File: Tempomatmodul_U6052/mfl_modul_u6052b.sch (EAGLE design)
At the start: 27 parts, among them IC1 U6052B-A, J1 43045-0800, K1 APF30212C, K2 APF30212C, K3 APF30212C, K4 APF30212C

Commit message: Fixed. Running version!
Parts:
- removed D6: P6KEXXC, diode:P6KEXXC
- removed R11, R12: 665, rcl:R-EU_0207/7
- removed R13: 931, rcl:R-EU_0207/7
- added C3: 100nF, rcl:C-EU025-025X050
- added LED1: led grün 2,2v 20mA, led:LED3MM
- C1: value 100µF -> 1nF
- C2: value 1nF -> 100uF/36V; device rcl:C-EU025-025X050 -> rcl:CPOL-EUE2.5-6
- D1: value BYW52 -> EP20D; device diode:BYW52 -> diode:DIODE-DO15-12
- D2, D3, D4, D5: value CGRM4004-G -> MBSR140; device diode:CGRM4004-G -> Heinrich:SHOTKY-SMDSMB
- J1: value 43045-0800 -> 39-30-1100; device Heinrich:43045-0800 -> Heinrich:39-30-1100
- R1: value 100 -> 560
- R10: value 200 -> 510
- R2: value 510 -> 100
- R3: value 200 -> 200k
- R4: value 270k -> 200
- R5: value 20k -> 931
- R6: value 150k -> 665
- R7: value 39k -> 665
- R8: value 200k -> 200
- R9: value 66.5 -> 66,5
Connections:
- net K1 renamed PLUS
- net K2 renamed ABRUF
- net K3 renamed MINUS
- net K4 renamed I/O
- removed net +12V: D1.C, D2.C, D3.C, D4.C, D5.C, K11.2, K21.2, K31.2, K41.2, R2.1, R3.1, R4.1, R6.1
- removed net LD: IC1.LD, R4.2, R5.2
- removed net MFL_CC: J1.5, R1.1
- removed net N$6: K12.S, K22.S, K32.S, K42.O, R11.1, R13.2
- removed net N$8: K22.P, R10.1
- removed net PO: IC1.PO, R6.2, R7.2
- new net IBUS: J1.3, J1.4
- new net MFL: J1.6, R2.1
- new net N$10: K22.P, R8.1
- new net N$11: K32.P, R7.1
- new net N$12: K12.S, K22.S, K32.S, K42.O, R5.2, R6.1
- new net N$3: LED1.A, R1.1
- new net VCC: D1.C, D2.C, D3.C, D4.C, D5.C, K11.2, K21.2, K31.2, K41.2, R1.2, R10.1, R4.1
- net EML1: now also J1.5, R6.2, R7.2, R8.2; no longer J1.8, R10.2, R11.2, R12.2
- net EML2: now also J1.10, R5.1; no longer J1.4, R13.1
- net GND: now also C2.-, C3.2, IC1.LD, IC1.PO, J1.7, J1.8, J1.9; no longer C2.2, D6.1, J1.2, J1.3, R5.1, R7.1
- net N$1: now also R2.2; no longer R1.2
- net N$2: now also R4.2; no longer R3.2
- net N$4: now also IC1.O8, LED1.C; no longer K32.P, R12.1
- net OSC: now also C1.1, R3.2; no longer C2.1, R8.2
- net VBAT: now also J1.1, J1.2; no longer D6.2, J1.6, J1.7
- net VS: now also C2.+, C3.1, R10.2; no longer C1.1, R2.2
- net VSTAB: now also R3.1; no longer R8.1
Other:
- note added: "logische Ausgänge, 25V und bis 200mA"
- note removed: "Abruf: Bit 1 und 4; 153Ohm Plus: Bit 2 und 5; 66.5Ohm Minus: Bit 7; 332Ohm Aus: 3 und 6; 1590Ohm Leerlauf: NICHTS; 665Ohm"
- note removed: "Anschlüße: 2x EML 2x 12V (rein und raus) 2x GND (rein und raus) 1x Tempomatsignal (rein)"
- note removed: "Wertetabelle: Abruf: K2 auf LOW Plus: K1 auf LOW Minus: K3 auf LOW Aus: K4 auf LOW Leerlauf: alle Relais auf HIGH"

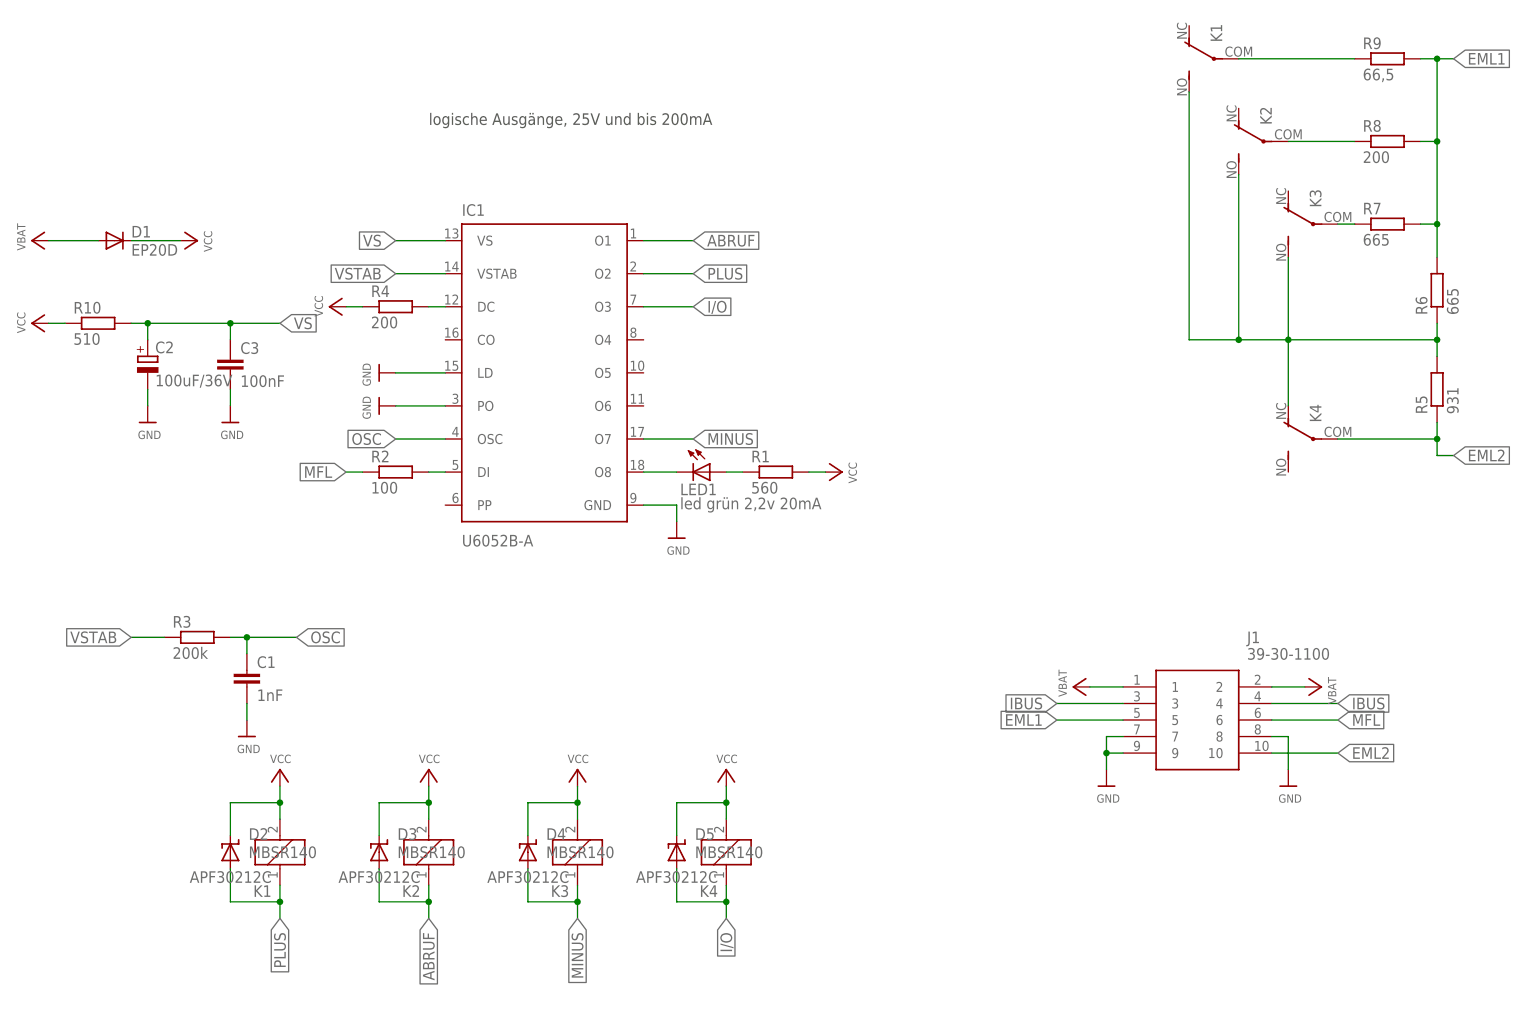
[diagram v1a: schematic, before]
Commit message: Fosc corrected
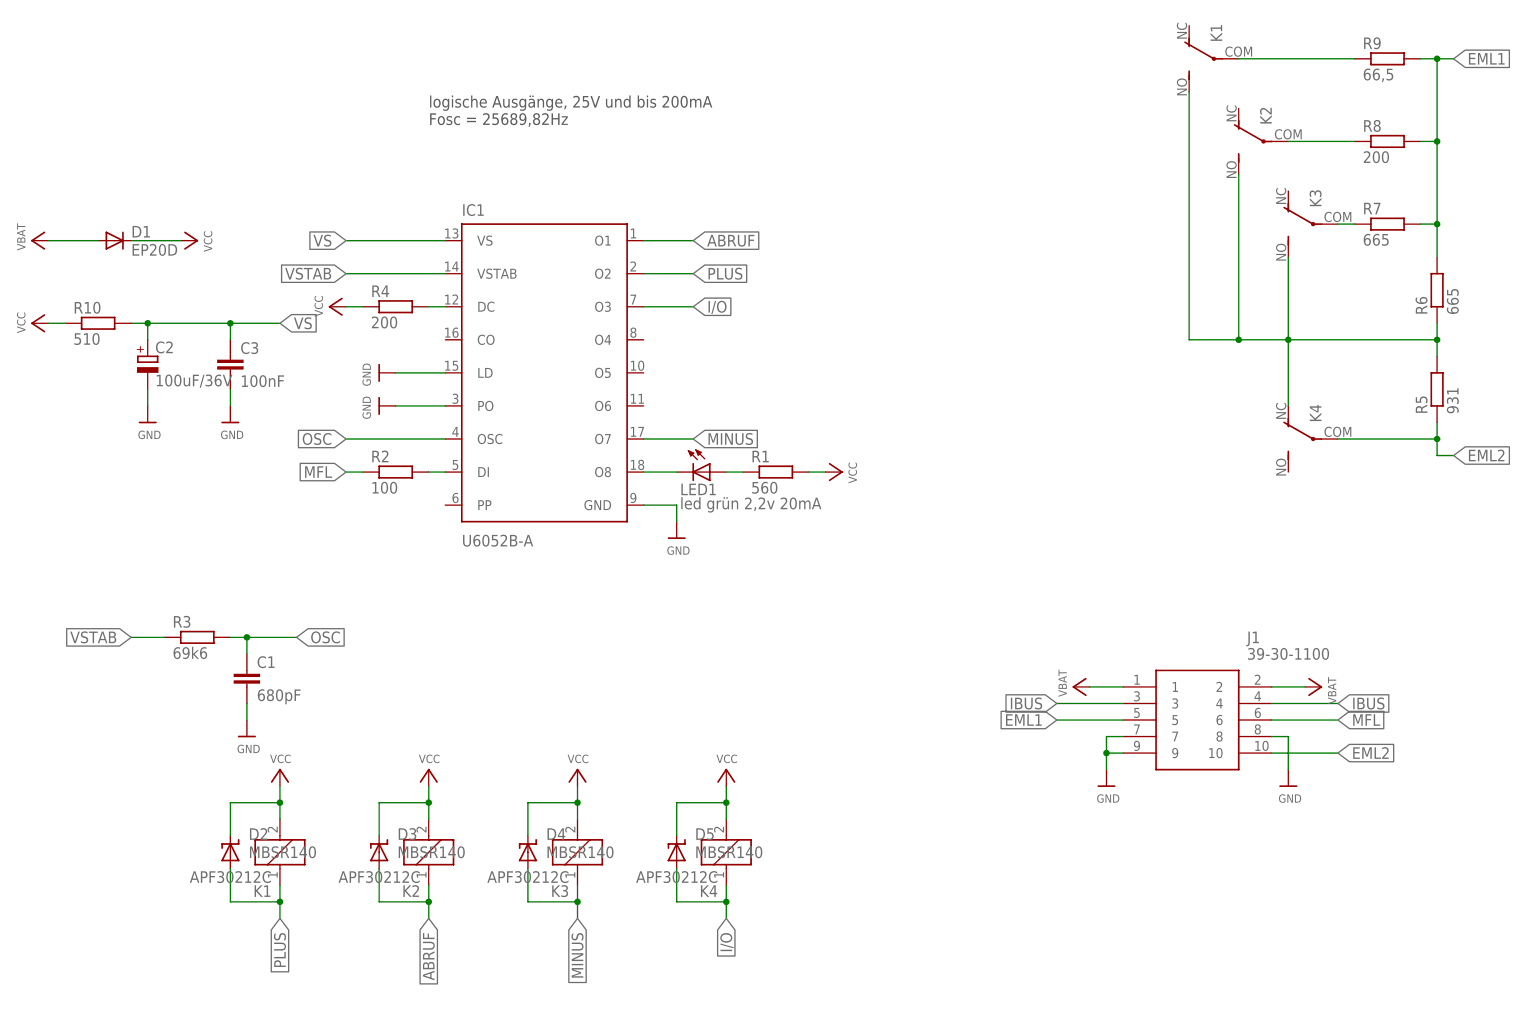
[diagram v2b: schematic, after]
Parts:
- C1: value 1nF -> 680pF
- R3: value 200k -> 69k6
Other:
- note added: "logische Ausgänge, 25V und bis 200mA Fosc = 25689,82Hz"
- note removed: "logische Ausgänge, 25V und bis 200mA"
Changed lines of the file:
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@@
 <setting verticaltext="up"/>
 </settings>
-<grid distance="0.1" unitdist="inch" unit="inch" style="lines" multiple="1" display="no" altdistance="0.01" altunitdist="inch" altunit="inch"/>
+<grid distance="0.1" unitdist="inch" unit="inch" style="lines" multiple="1" display="yes" altdistance="0.01" altunitdist="inch" altunit="inch"/>
 <layers>
 <layer number="1" name="Top" color="4" fill="1" visible="no" active="no"/>
@@
 <part name="R1" library="rcl" library_urn="urn:adsk.eagle:library:334" deviceset="R-EU_" device="0207/7" package3d_urn="urn:adsk.eagle:package:23493/1" value="560"/>
 <part name="P+1" library="microbuilder" deviceset="VCC" device=""/>
-<part name="C1" library="rcl" library_urn="urn:adsk.eagle:library:334" deviceset="C-EU" device="025-025X050" package3d_urn="urn:adsk.eagle:package:23629/2" value="1nF"/>
+<part name="C1" library="rcl" library_urn="urn:adsk.eagle:library:334" deviceset="C-EU" device="025-025X050" package3d_urn="urn:adsk.eagle:package:23629/2" value="680pF"/>
 <part name="R2" library="rcl" library_urn="urn:adsk.eagle:library:334" deviceset="R-EU_" device="0207/7" package3d_urn="urn:adsk.eagle:package:23493/1" value="100"/>
-<part name="R3" library="rcl" library_urn="urn:adsk.eagle:library:334" deviceset="R-EU_" device="0207/7" package3d_urn="urn:adsk.eagle:package:23493/1" value="200k"/>
+<part name="R3" library="rcl" library_urn="urn:adsk.eagle:library:334" deviceset="R-EU_" device="0207/7" package3d_urn="urn:adsk.eagle:package:23493/1" value="69k6"/>
 <part name="R4" library="rcl" library_urn="urn:adsk.eagle:library:334" deviceset="R-EU_" device="0207/7" package3d_urn="urn:adsk.eagle:package:23493/1" value="200"/>
 <part name="R5" library="rcl" library_urn="urn:adsk.eagle:library:334" deviceset="R-EU_" device="0207/7" package3d_urn="urn:adsk.eagle:package:23493/1" value="931"/>
@@
 <sheet>
 <plain>
-<text x="83.82" y="147.32" size="1.778" layer="97">logische Ausgänge, 25V und bis 200mA</text>
+<text x="83.82" y="147.32" size="1.778" layer="97">logische Ausgänge, 25V und bis 200mA
+Fosc = 25689,82Hz</text>
 </plain>
 <instances>
@@
 <segment>
 <pinref part="IC1" gate="G$1" pin="OSC"/>
-<wire x1="86.36" y1="99.06" x2="78.74" y2="99.06" width="0.1524" layer="91"/>
-<label x="78.74" y="99.06" size="1.778" layer="95" rot="R180" xref="yes"/>
+<wire x1="86.36" y1="99.06" x2="71.12" y2="99.06" width="0.1524" layer="91"/>
+<label x="71.12" y="99.06" size="1.778" layer="95" rot="R180" xref="yes"/>
 </segment>
 <segment>
@@
 <segment>
 <pinref part="IC1" gate="G$1" pin="VS"/>
-<wire x1="86.36" y1="129.54" x2="78.74" y2="129.54" width="0.1524" layer="91"/>
-<label x="78.74" y="129.54" size="1.778" layer="95" rot="R180" xref="yes"/>
+<wire x1="86.36" y1="129.54" x2="71.12" y2="129.54" width="0.1524" layer="91"/>
+<label x="71.12" y="129.54" size="1.778" layer="95" rot="R180" xref="yes"/>
 </segment>
 <segment>
@@
 <segment>
 <pinref part="IC1" gate="G$1" pin="VSTAB"/>
-<wire x1="86.36" y1="124.46" x2="78.74" y2="124.46" width="0.1524" layer="91"/>
-<label x="78.74" y="124.46" size="1.778" layer="95" rot="R180" xref="yes"/>
+<wire x1="86.36" y1="124.46" x2="71.12" y2="124.46" width="0.1524" layer="91"/>
+<label x="71.12" y="124.46" size="1.778" layer="95" rot="R180" xref="yes"/>
 </segment>
 <segment>
@@
 </drawing>
 <compatibility>
+<note version="6.3" minversion="6.2.2" severity="warning">
+Since Version 6.2.2 text objects can contain more than one line,
+which will not be processed correctly with this version.
+</note>
 <note version="8.2" severity="warning">
 Since Version 8.2, EAGLE supports online libraries. The ids

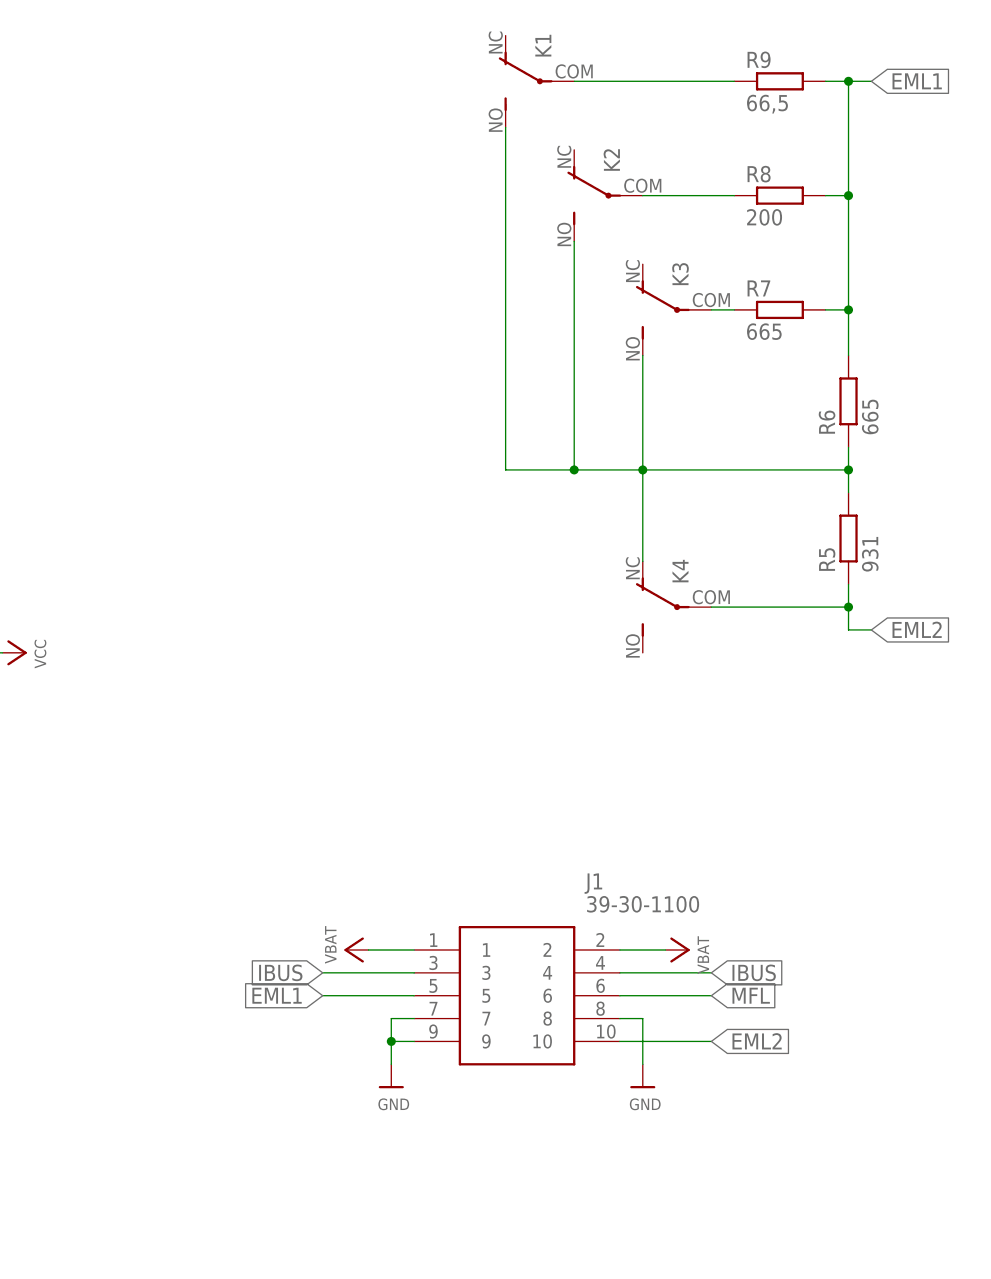
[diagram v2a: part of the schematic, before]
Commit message: Added support for V8 engines (M60 and M62)
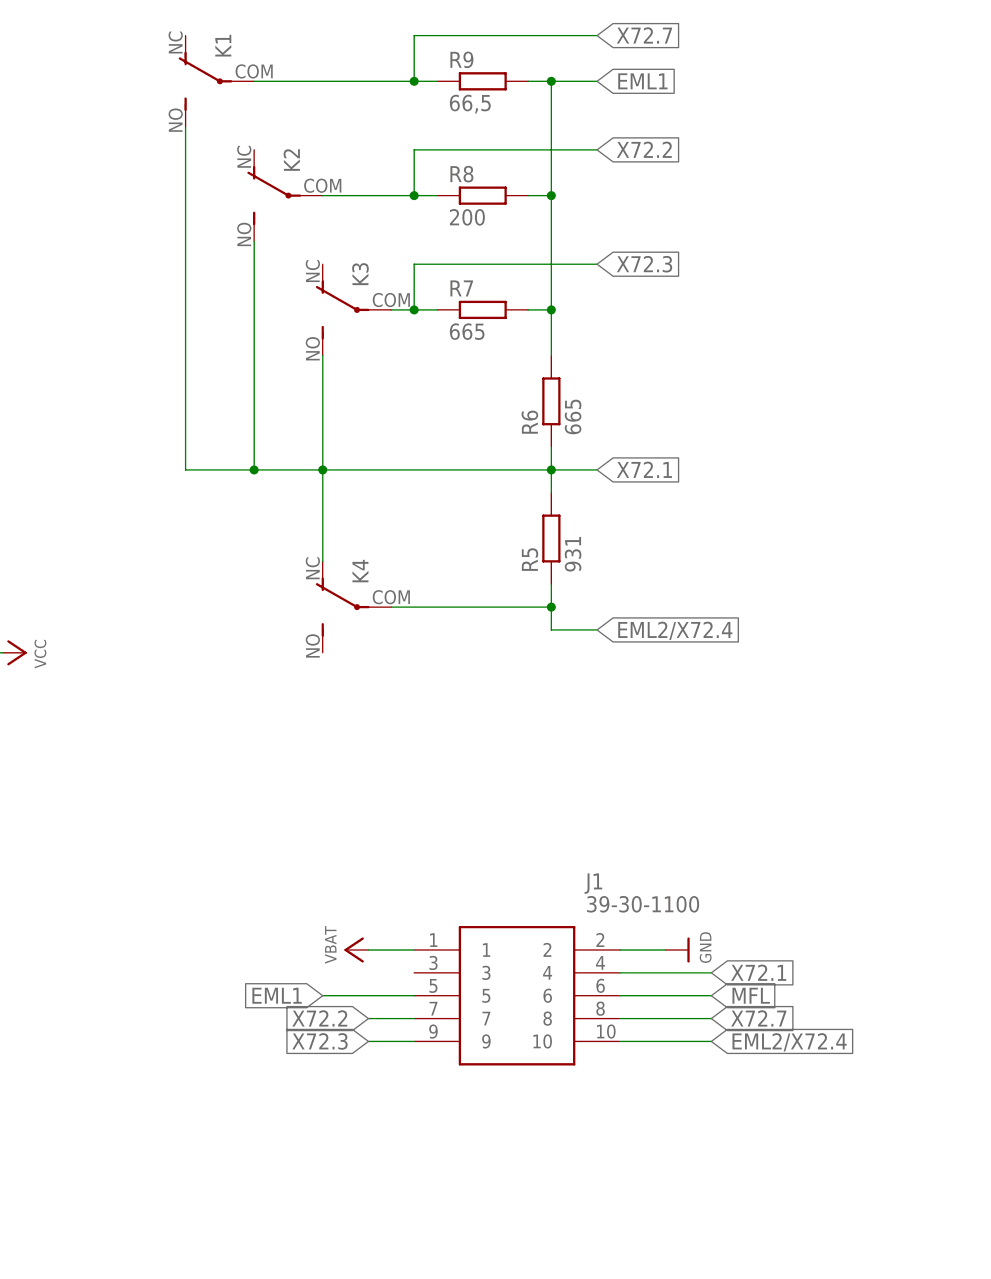
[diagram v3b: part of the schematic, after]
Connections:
- net EML2 renamed EML2/X72.4
- removed net IBUS: J1.3, J1.4
- removed net N$10: K22.P, R8.1
- removed net N$11: K32.P, R7.1
- removed net N$12: K12.S, K22.S, K32.S, K42.O, R5.2, R6.1
- removed net N$9: K12.P, R9.1
- new net X72.1: J1.4, K12.S, K22.S, K32.S, K42.O, R5.2, R6.1
- new net X72.2: J1.7, K22.P, R8.1
- new net X72.3: J1.9, K32.P, R7.1
- new net X72.7: J1.8, K12.P, R9.1
- net GND: now also J1.2; no longer J1.7, J1.8, J1.9
- net VBAT: no longer J1.2
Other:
- moved on the sheet: K1, K2, K3, K4, R5, R6, R7, R8, R9

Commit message: refactoring
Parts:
- R3: value 69k6 -> 69k8
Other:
- note added: "logische Ausgänge, 25V und bis 200mA Fosc = 25619,111Hz"
- note removed: "logische Ausgänge, 25V und bis 200mA Fosc = 25689,82Hz"
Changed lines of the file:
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@@
 <part name="C1" library="rcl" library_urn="urn:adsk.eagle:library:334" deviceset="C-EU" device="025-025X050" package3d_urn="urn:adsk.eagle:package:23629/2" value="680pF"/>
 <part name="R2" library="rcl" library_urn="urn:adsk.eagle:library:334" deviceset="R-EU_" device="0207/7" package3d_urn="urn:adsk.eagle:package:23493/1" value="100"/>
-<part name="R3" library="rcl" library_urn="urn:adsk.eagle:library:334" deviceset="R-EU_" device="0207/7" package3d_urn="urn:adsk.eagle:package:23493/1" value="69k6"/>
+<part name="R3" library="rcl" library_urn="urn:adsk.eagle:library:334" deviceset="R-EU_" device="0207/7" package3d_urn="urn:adsk.eagle:package:23493/1" value="69k8"/>
 <part name="R4" library="rcl" library_urn="urn:adsk.eagle:library:334" deviceset="R-EU_" device="0207/7" package3d_urn="urn:adsk.eagle:package:23493/1" value="200"/>
 <part name="R5" library="rcl" library_urn="urn:adsk.eagle:library:334" deviceset="R-EU_" device="0207/7" package3d_urn="urn:adsk.eagle:package:23493/1" value="931"/>
@@
 <plain>
 <text x="83.82" y="147.32" size="1.778" layer="97">logische Ausgänge, 25V und bis 200mA
-Fosc = 25689,82Hz</text>
+Fosc = 25619,111Hz</text>
 </plain>
 <instances>
